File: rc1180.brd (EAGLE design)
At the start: 30 x 49.5 mm, 19 parts, among them J1 47642-0001, U1 CH340C, U2 AMS1117, X1 SMA-142-0701-801/806

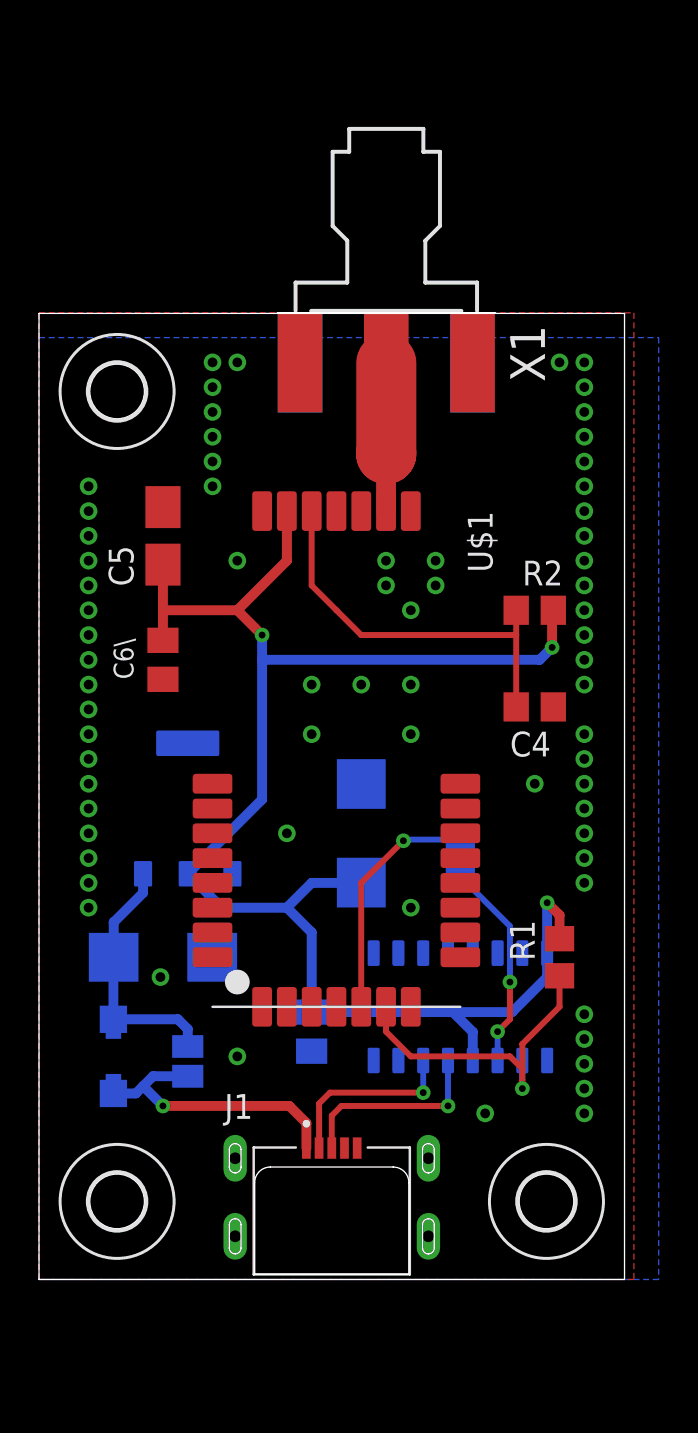
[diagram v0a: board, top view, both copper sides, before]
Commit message: Extended board to 54 mm for easy soldering of rf connector
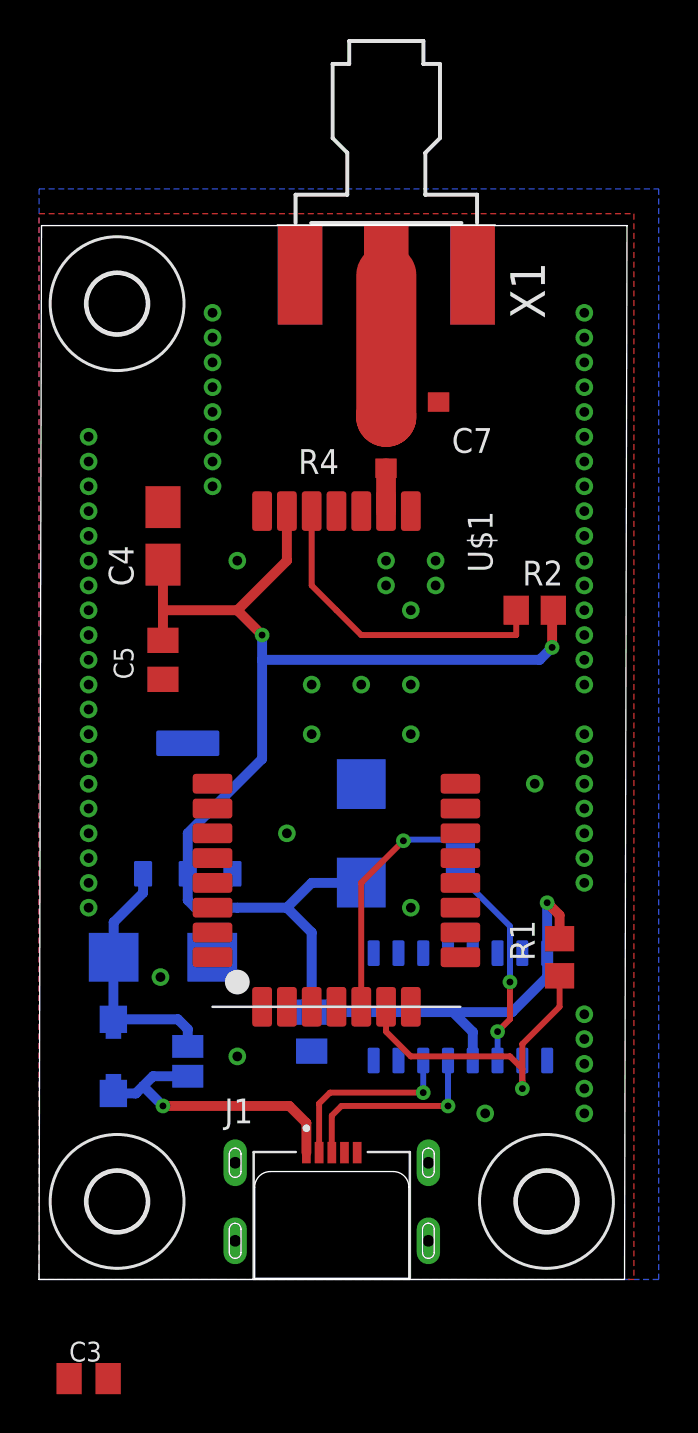
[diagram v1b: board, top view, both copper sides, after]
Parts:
- removed C6\: 100nF, rcl:C0805K
- added C2: 22uF, rcl:C/6032-28R
- added C6: 100nF, rcl:C0805K
- added R4: TBD, rcl:R0603
- C3: value 22uF -> 100nF; device rcl:C/6032-28R -> rcl:C0805K
- C4: value 100nF -> 2u2F; device rcl:C0805 -> rcl:A/3216-18W
- C5: value 2u2F -> 100nF; device rcl:A/3216-18W -> rcl:C0805K
- C7: value 100nF -> TBD; device rcl:C0805K -> rcl:C0603
- H1, H2, H3: value MOUNT-HOLE2.8 -> MOUNT-HOLE3.0; device holes:2,8 -> holes:3,0
- moved C7 32.7 mm to (19.6, 45.0), flipped to the top, turned to 0 degrees
- moved C3 31.2 mm to (2.54, -5.08), flipped to the top, turned to 0 degrees
- moved C4 21.0 mm to (6.35, 38.1), turned to 270 degrees
- moved C5 6.35 mm to (6.35, 31.8), turned to 90 degrees
- moved X1 4.50 mm to (17.8, 54.0)
- moved H3 4.50 mm to (4.00, 50.0)
- moved J1 0.23 mm to (15.0, 6.50)
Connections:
- new net N$3: C7.1, R4.2, X1.1
- net +3V3: now also C2.+, C4.+, C5.2, C6.2; no longer C3.+, C5.+, C6\.2, C7.2
- net GND: now also C2.-, C3.1, C4.-, C5.1, C6.1, C7.2; no longer C3.-, C4.2, C5.-, C6\.1, C7.1
- net RC_ANT: now also R4.1; no longer X1.1
- net RC_RESET: now also C3.2; no longer C4.1
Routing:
- net N$3: track 0.00 -> 7.28 mm
- net RC_ANT: track 7.60 -> 2.20 mm
- net RC_RESET: track 20.3 -> 16.6 mm
- net +3V3: track 84.1 -> 84.9 mm
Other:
- board size 30 x 49.5 mm -> 30.1 x 54 mm
- board text added: "RC1180 REV 1.0 https://github.com/jacek27/rc1180_dongle"

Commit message: Connected the 100nF updated cap
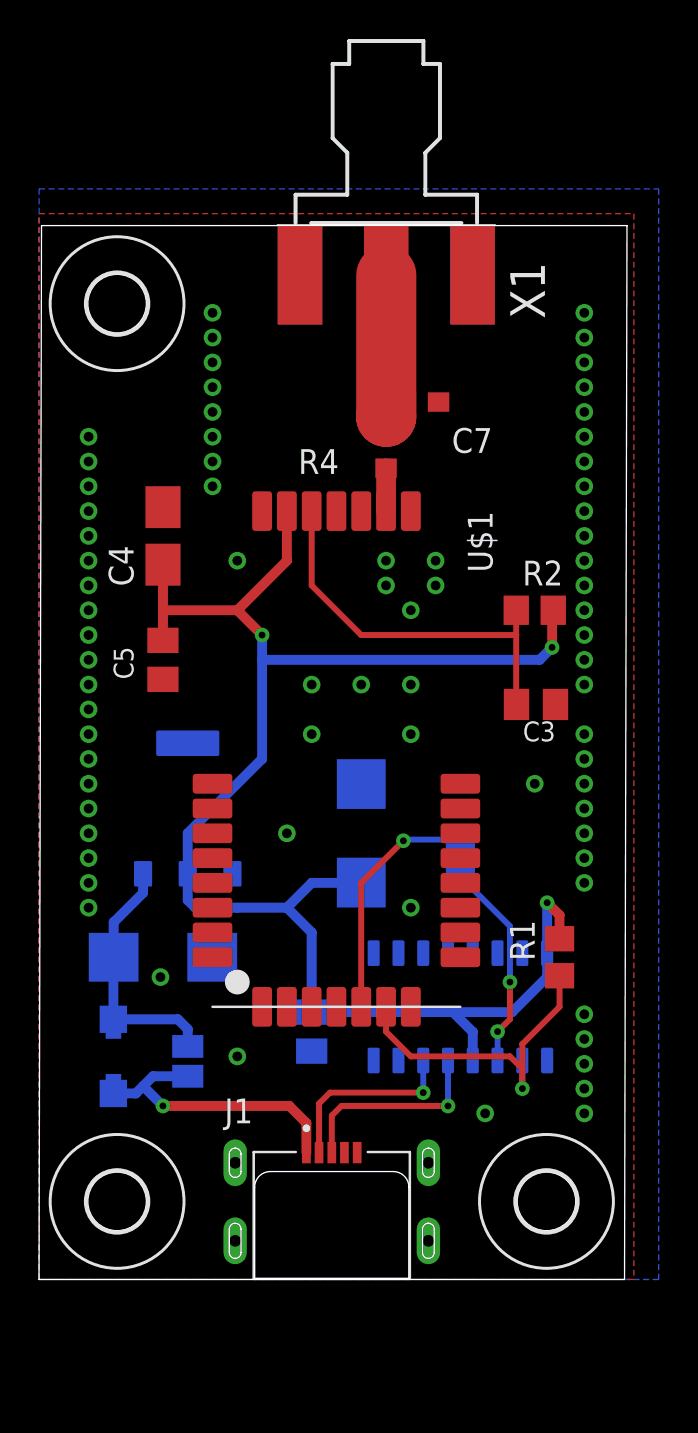
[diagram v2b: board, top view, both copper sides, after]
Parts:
- moved C3 41.5 mm to (25.5, 29.5), turned to 180 degrees
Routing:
- net RC_RESET: track 16.6 -> 20.2 mm
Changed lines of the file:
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@@
 <attribute name="VALUE" x="18.9865" y="43.053" size="1.27" layer="27"/>
 </element>
-<element name="C3" library="rcl" library_urn="urn:adsk.eagle:library:334" package="C0805K" package3d_urn="urn:adsk.eagle:package:23681/2" value="100nF" x="2.54" y="-5.08" smashed="yes">
-<attribute name="NAME" x="1.54" y="-4.205" size="1.016" layer="25"/>
-<attribute name="POPULARITY" value="52" x="2.54" y="-5.08" size="1.778" layer="27" display="off"/>
-<attribute name="SPICEPREFIX" value="C" x="2.54" y="-5.08" size="1.778" layer="27" display="off"/>
-<attribute name="VALUE" x="1.54" y="-6.98" size="1.016" layer="27"/>
+<element name="C3" library="rcl" library_urn="urn:adsk.eagle:library:334" package="C0805K" package3d_urn="urn:adsk.eagle:package:23681/2" value="100nF" x="25.4635" y="29.464" smashed="yes" rot="R180">
+<attribute name="NAME" x="26.4635" y="28.589" size="1.016" layer="25" rot="R180"/>
+<attribute name="POPULARITY" value="52" x="25.4635" y="29.464" size="1.778" layer="27" rot="R180" display="off"/>
+<attribute name="SPICEPREFIX" value="C" x="25.4635" y="29.464" size="1.778" layer="27" rot="R180" display="off"/>
+<attribute name="VALUE" x="26.4635" y="31.364" size="1.016" layer="27" rot="R180"/>
 </element>
 </elements>
@@
 <via x="2.54" y="43.18" extent="1-16" drill="0.5"/>
 <contactref element="C3" pad="1"/>
-<wire x1="10.05" y1="1.98" x2="1.54" y2="-5.08" width="0" layer="19" extent="1-1"/>
 </signal>
 <signal name="+3V3">
@@
 <contactref element="R2" pad="1"/>
 <wire x1="13.97" y1="39.37" x2="13.97" y2="35.56" width="0.3048" layer="1"/>
-<wire x1="13.97" y1="35.56" x2="15.24" y2="34.29" width="0.3048" layer="1"/>
-<wire x1="24.45" y1="33.02" x2="24.45" y2="34.29" width="0.3048" layer="1"/>
+<wire x1="24.45" y1="34.29" x2="24.45" y2="33.02" width="0.3048" layer="1"/>
 <wire x1="24.45" y1="33.02" x2="16.51" y2="33.02" width="0.3048" layer="1"/>
-<wire x1="16.51" y1="33.02" x2="15.24" y2="34.29" width="0.3048" layer="1"/>
+<wire x1="16.51" y1="33.02" x2="13.97" y2="35.56" width="0.3048" layer="1"/>
 <contactref element="C3" pad="2"/>
-<wire x1="3.54" y1="-5.08" x2="24.45" y2="34.29" width="0" layer="19" extent="1-1"/>
+<wire x1="24.45" y1="33.02" x2="24.45" y2="29.4775" width="0.3048" layer="1"/>
+<wire x1="24.45" y1="29.4775" x2="24.4635" y2="29.464" width="0.3048" layer="1"/>
 </signal>
 <signal name="N$1">

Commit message: Added vias and testpoints
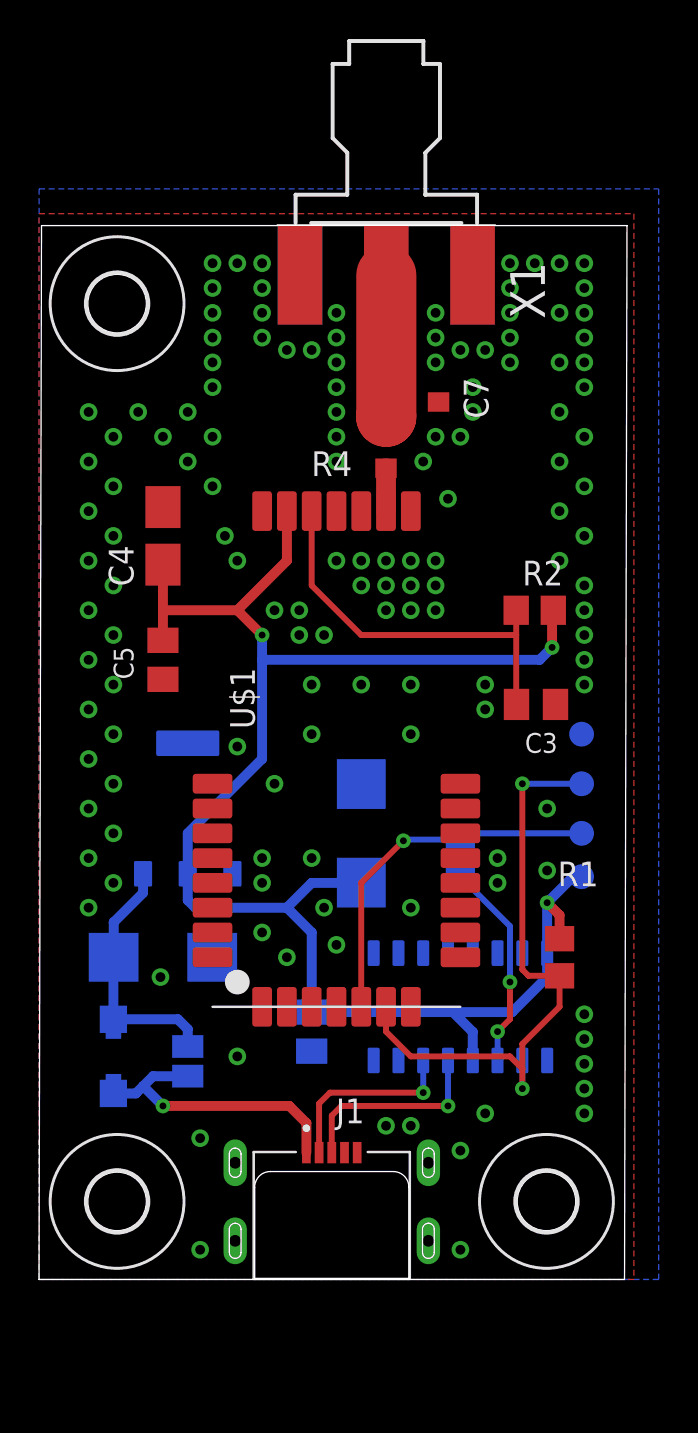
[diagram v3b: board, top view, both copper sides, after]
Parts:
- added 3V3, GND, RC_RXD, RC_TXD: TPB1,27, testpad:B1,27
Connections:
- net +3V3: now also 3V3.TP
- net GND: now also GND.TP
- net RC_RXD: now also RC_RXD.TP
- net RC_TXD: now also RC_TXD.TP
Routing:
- net RC_RXD: track 17.1 -> 31.7 mm, vias 1 -> 2
- net RC_TXD: track 12.3 -> 18.7 mm
- net +3V3: track 84.9 -> 87.2 mm
